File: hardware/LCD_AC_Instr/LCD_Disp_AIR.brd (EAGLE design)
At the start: 58.4 x 58.4 mm, 38 parts, among them IC3 TC10553.3V, J1 12V input, Q1 16MHz, SW1 ENCODER_SW1-PEC12, U1 ATMEGA328P-AU(R), U3 78M05

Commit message: changed resistor value in i2C lines to 100K to allow for the old style BMP085 which is not 5V compatible
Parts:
- R7, R8: value 1k -> 100k
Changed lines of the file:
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@@
 <attribute name="NAME" x="41.8592" y="51.816" size="1.27" layer="25" font="vector" ratio="10" rot="R90"/>
 </element>
-<element name="R7" library="dp_devices" package="R603" value="1k" x="12.0716625" y="40.01515" smashed="yes" rot="MR270">
+<element name="R7" library="dp_devices" package="R603" value="100k" x="12.0716625" y="40.01515" smashed="yes" rot="MR270">
 <attribute name="NAME" x="12.3256625" y="38.23715" size="1.016" layer="26" font="vector" ratio="10" rot="MR270"/>
 <attribute name="VALUE" x="12.4526625" y="43.31715" size="1.27" layer="28" font="vector" ratio="10" rot="MR270"/>
 </element>
-<element name="R8" library="dp_devices" package="R603" value="1k" x="14.601640625" y="40.00259375" smashed="yes" rot="MR270">
+<element name="R8" library="dp_devices" package="R603" value="100k" x="14.601640625" y="40.00259375" smashed="yes" rot="MR270">
 <attribute name="NAME" x="14.855640625" y="38.22459375" size="1.016" layer="26" font="vector" ratio="10" rot="MR270"/>
 <attribute name="VALUE" x="14.982640625" y="43.30459375" size="1.016" layer="28" font="vector" ratio="10" rot="MR270"/>

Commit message: Added Geiger counter schematic and layout Added copy arduino sketch from rhelectronics
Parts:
- F1: value (none) -> 4A
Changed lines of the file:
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@@
 <attribute name="VALUE" x="20.32" y="28.575" size="1.27" layer="28" rot="MR90"/>
 </element>
-<element name="F1" library="dp_devices" package="PTC0805" value="" x="22.86" y="5.3975"/>
+<element name="F1" library="dp_devices" package="PTC0805" value="4A" x="22.86" y="5.3975"/>
 <element name="LCD-BL" library="1AA_Stofer" package="1X02" value="" x="21.59" y="51.435" rot="MR270"/>
 </elements>

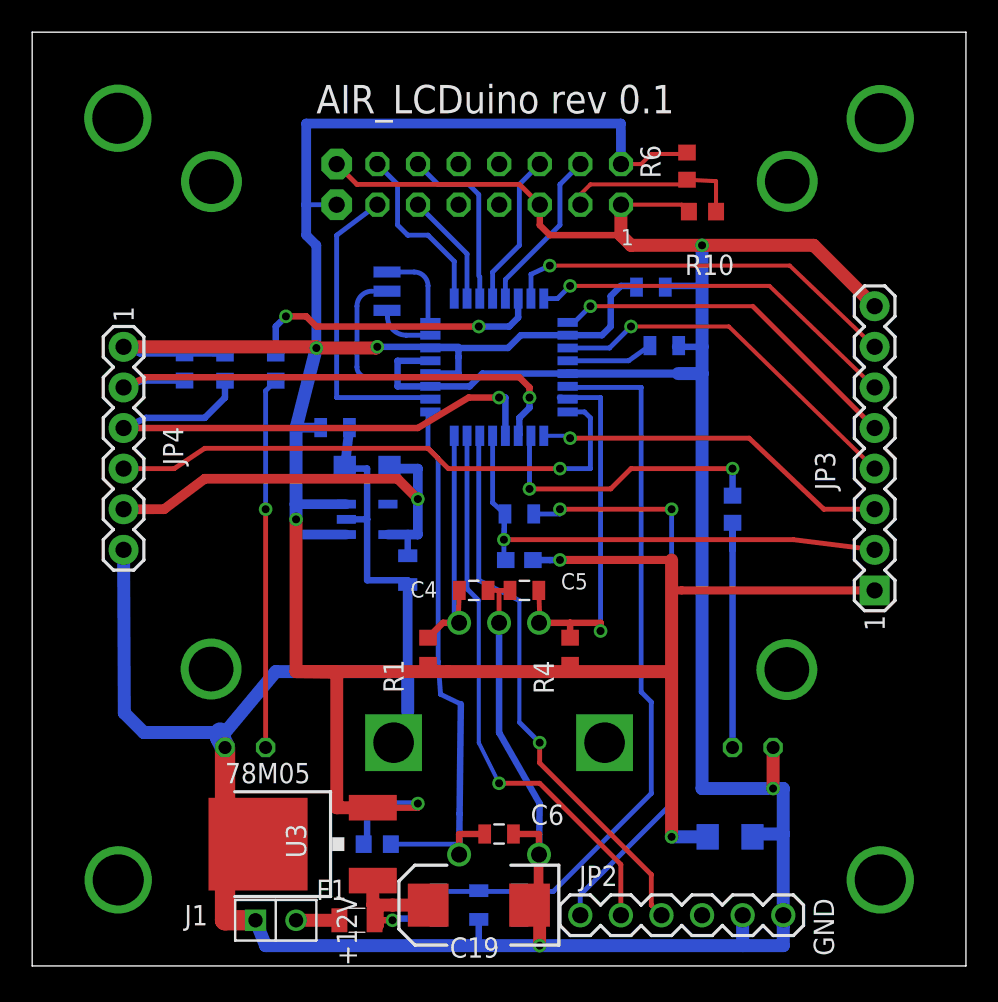
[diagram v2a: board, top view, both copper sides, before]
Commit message: added 12_adc_daughter/LTC2495_16x_pga_adc.pdf removed eagle.epf files and added gitignore file
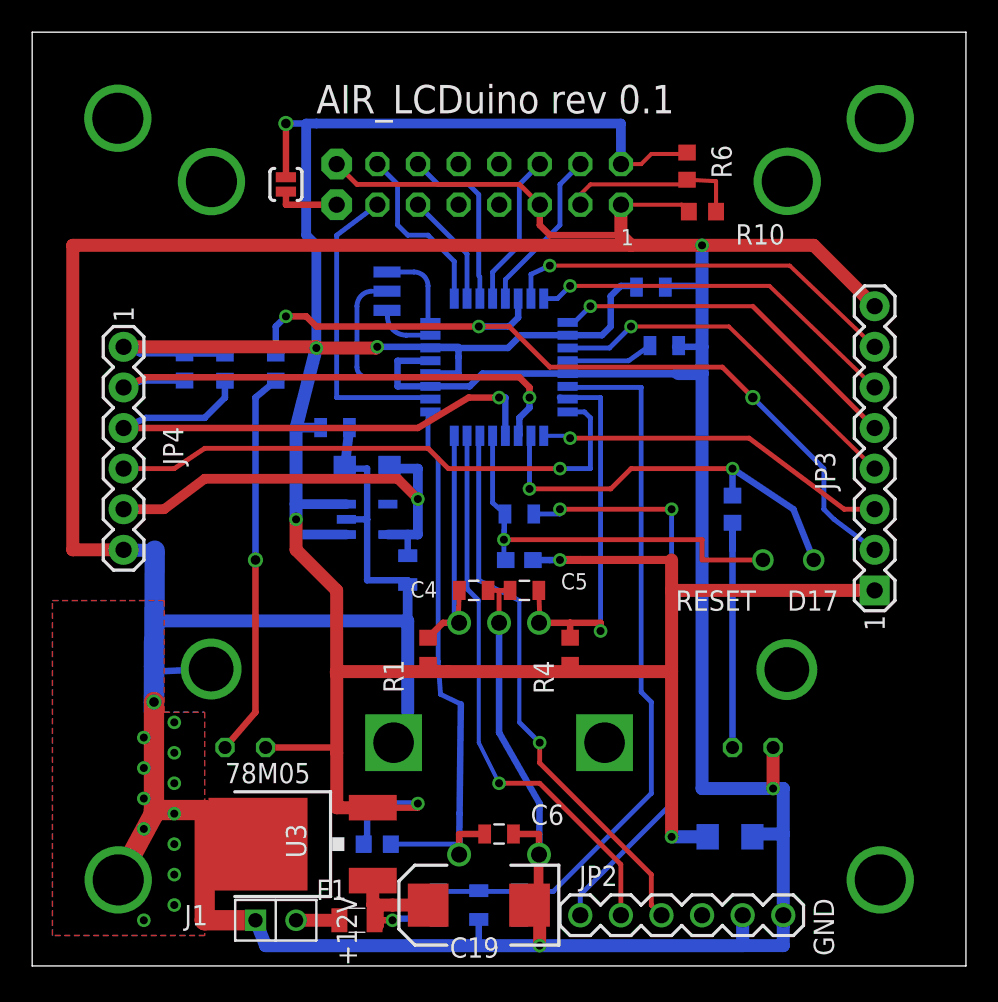
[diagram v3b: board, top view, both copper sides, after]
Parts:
- added D17: D17-A3-PC3, 1AA_Stofer:P1-13
- added RESET: SOLDER_POINTA, 1AA_Stofer:P1-13
- added SJ1: BACKLIGHT, SparkFun-Passives:SJ_2S-NO
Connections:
- removed net D10_PB2: R2.2, U1.14
- new net D10_PB2_SS: JP3.2, R2.2, U1.14
- new net N$12: LED1.K, R2.1
- net 5V: now also LED1.A, SJ1.1; no longer LCD-BL.2
- net A3_PC3: now also D17.1
- net GND: no longer LED1.K
- net N$13: now also LCD-BL.2, SJ1.2; no longer LED1.A, R2.1
- net RESET: now also RESET.1; no longer JP3.2
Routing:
- net GND: track 273.0 -> 356.2 mm, vias 3 -> 18
- net D10_PB2_SS: track 0.00 -> 50.7 mm, vias 0 -> 3
- net N$12: track 0.00 -> 24.3 mm, vias 0 -> 1
- net N$13: track 23.2 -> 4.00 mm, vias 1 -> 0
- net D10_PB2: track 18.8 -> 0.00 mm, vias 2 -> 0
- net 5V: track 209.9 -> 219.8 mm, vias 6 -> 7
- net A3_PC3: track 18.3 -> 26.3 mm
- net RESET: track 33.1 -> 27.3 mm
- added copper zone on layer 1, net GND
- added copper zone on layer 16, net GND
